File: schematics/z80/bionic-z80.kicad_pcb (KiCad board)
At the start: 2 copper layers, 25.4 x 68.6 mm, 8 parts, among them J1 Bionic-P135, J2 Bionic-P245, U1 Z84C00, U2 11AA010-I/TT

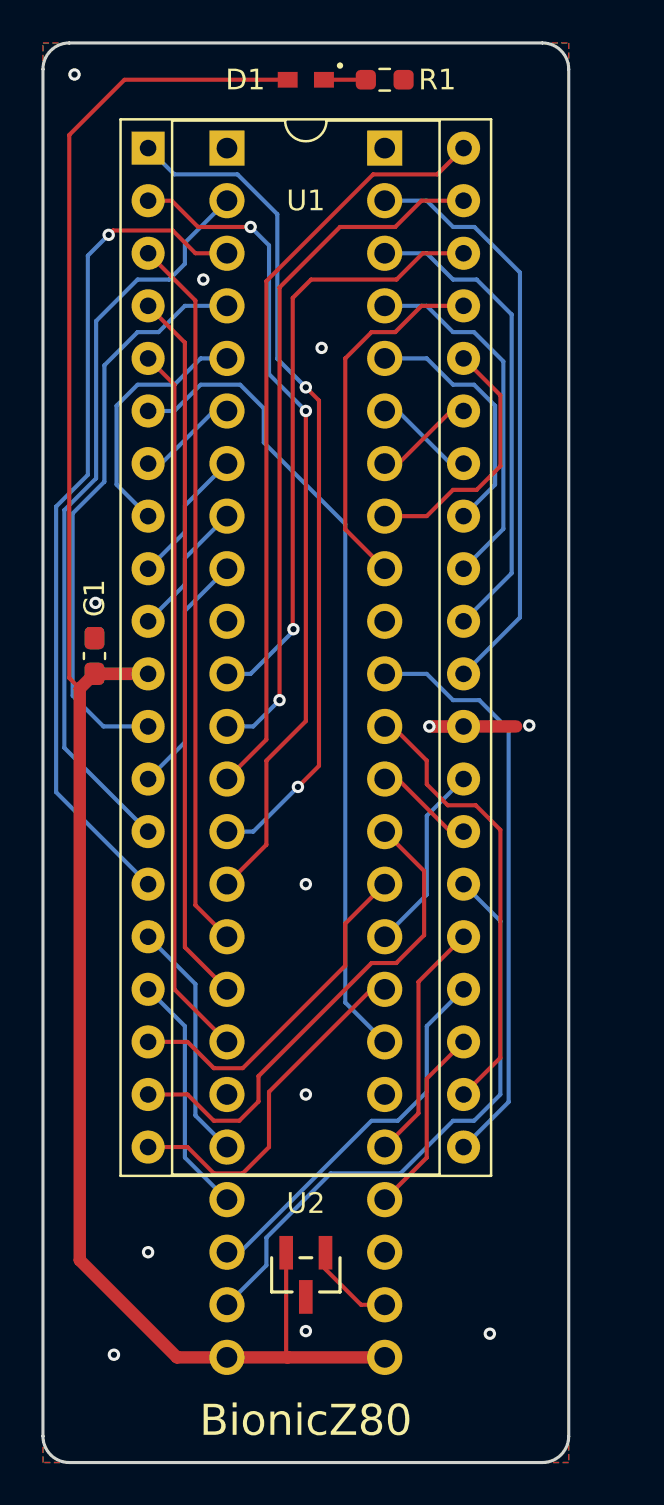
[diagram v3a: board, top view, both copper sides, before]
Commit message: [Z80] Cleanup schematics
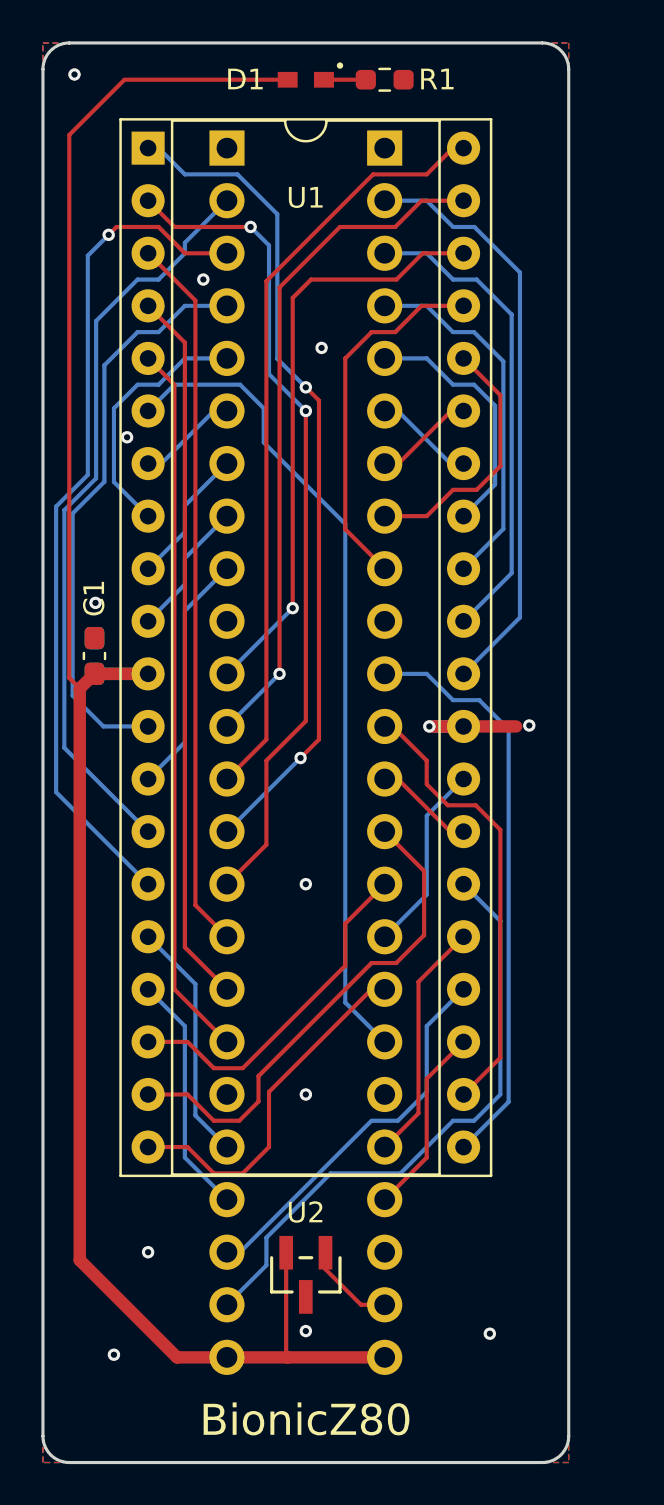
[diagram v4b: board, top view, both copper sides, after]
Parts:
- D1: footprint 0-LocalLibrary:LED_CSL1901UW1_ROM-M -> rhom:LED_CSL1901UW1_ROM-M
- J1: footprint 0-LocalLibrary:Bionic-P135_Vertical -> bionic:Bionic-P135_Vertical
- J2: footprint 0-LocalLibrary:Bionic-P245_Vertical -> bionic:Bionic-P245_Vertical
- U1: footprint 0-LocalLibrary:DIP-40_W15.24mm_Socket -> bionic:DIP-40_W15.24mm_Socket
- U2: footprint 0-LocalLibrary:SOT-23_MC_MCH-M -> microchip:SOT-23_MC_MCH-M
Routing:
- net /P33: track 40.8 -> 40.1 mm
- net /P31: track 33.6 -> 32.9 mm
- net /P30: track 29.3 -> 28.6 mm
- net GND: vias 12 -> 13
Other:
- rule pad_to_mask_clearance: 0.051 -> 0

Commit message: [Z80] Update schematics
Remove unused pins from bionic connector
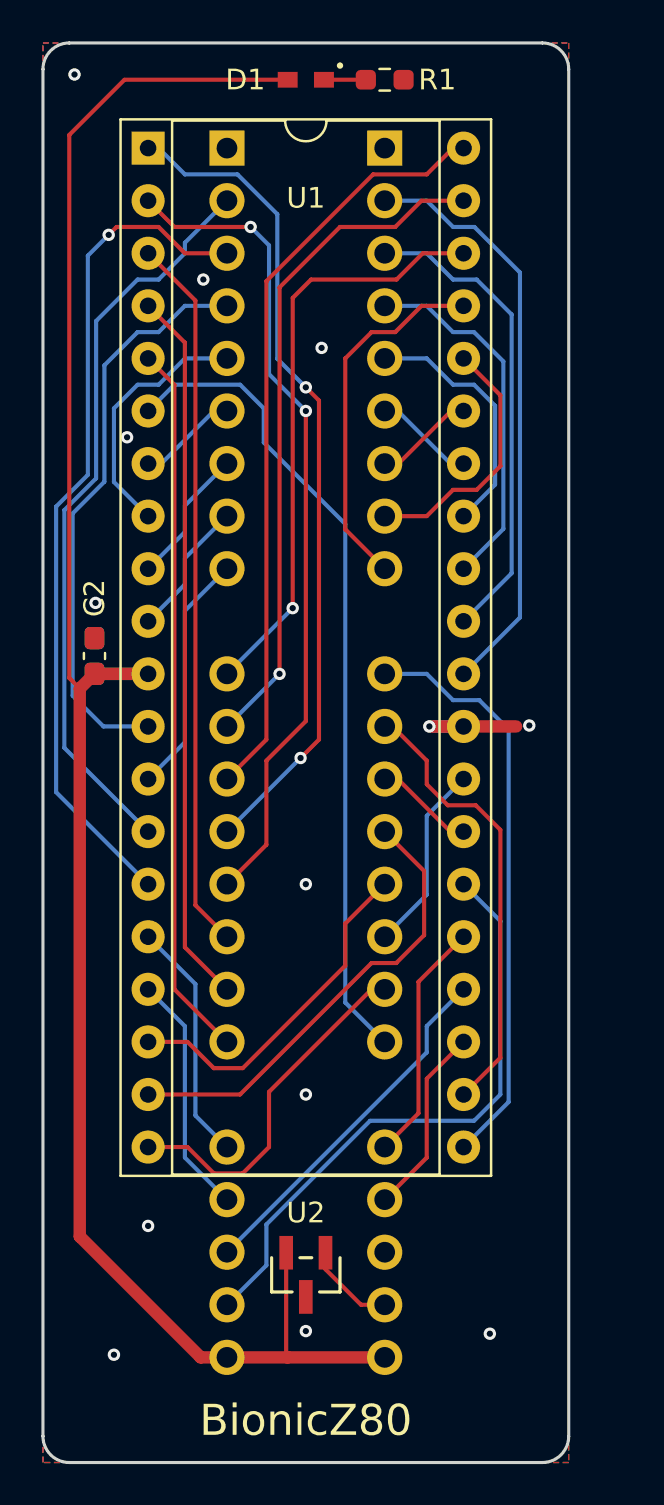
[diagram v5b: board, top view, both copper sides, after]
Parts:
- C1: moved to B.Cu
- C2: moved to F.Cu
- J1: footprint bionic:Bionic-P135_Vertical -> bionic:Bionic-P135_THT
- J2: footprint bionic:Bionic-P245_Vertical -> bionic:Bionic-P245_THT
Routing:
- net /P43: track 24.1 -> 22.3 mm
- net /P52: track 18.6 -> 17.4 mm
- net VCC: track 94.2 -> 93.5 mm
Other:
- board text added: "Rev. 4"
- board text removed: "Rev. 3"
